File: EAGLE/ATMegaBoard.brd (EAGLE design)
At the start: 71.1 x 54.3 mm, 31 parts, among them IC1 L298, IC2 ATMEGA168-20P, IC3 REG1117, X1 49S/18PF

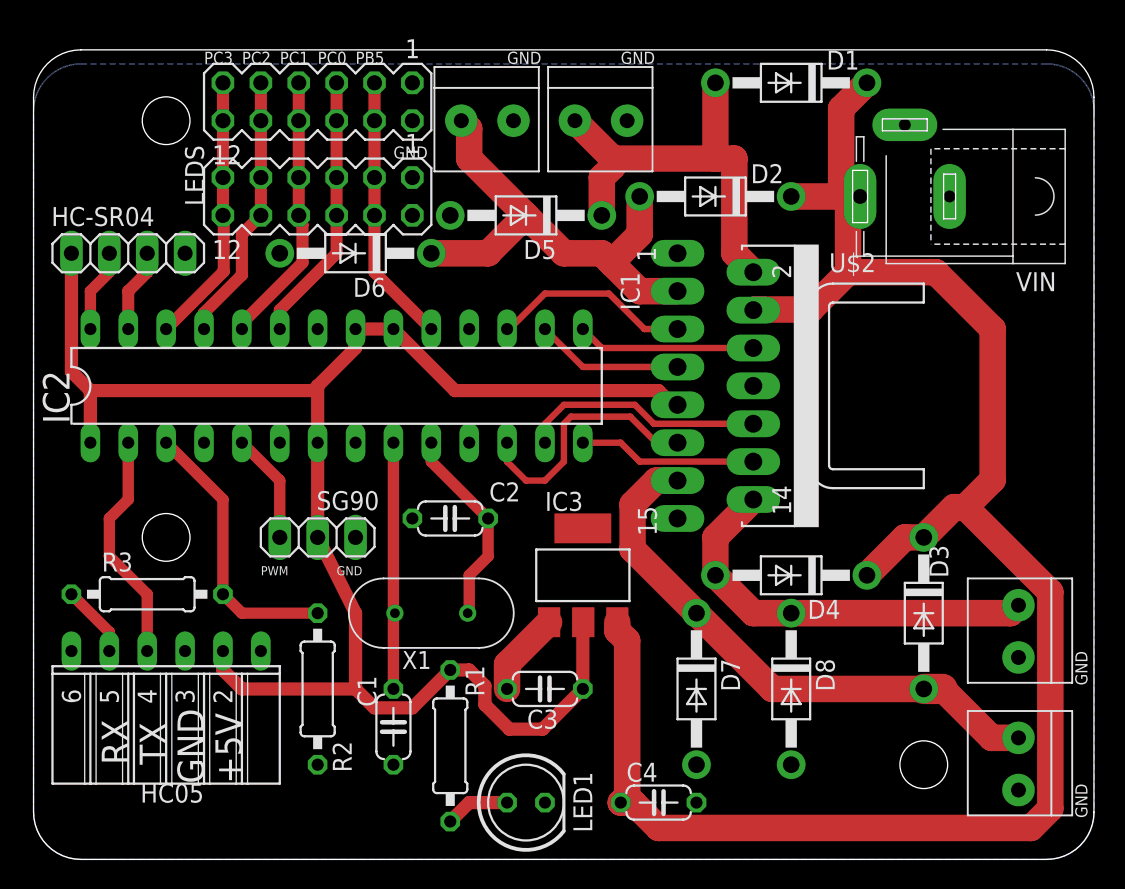
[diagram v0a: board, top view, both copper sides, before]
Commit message: increased clearance between LEDs and D6
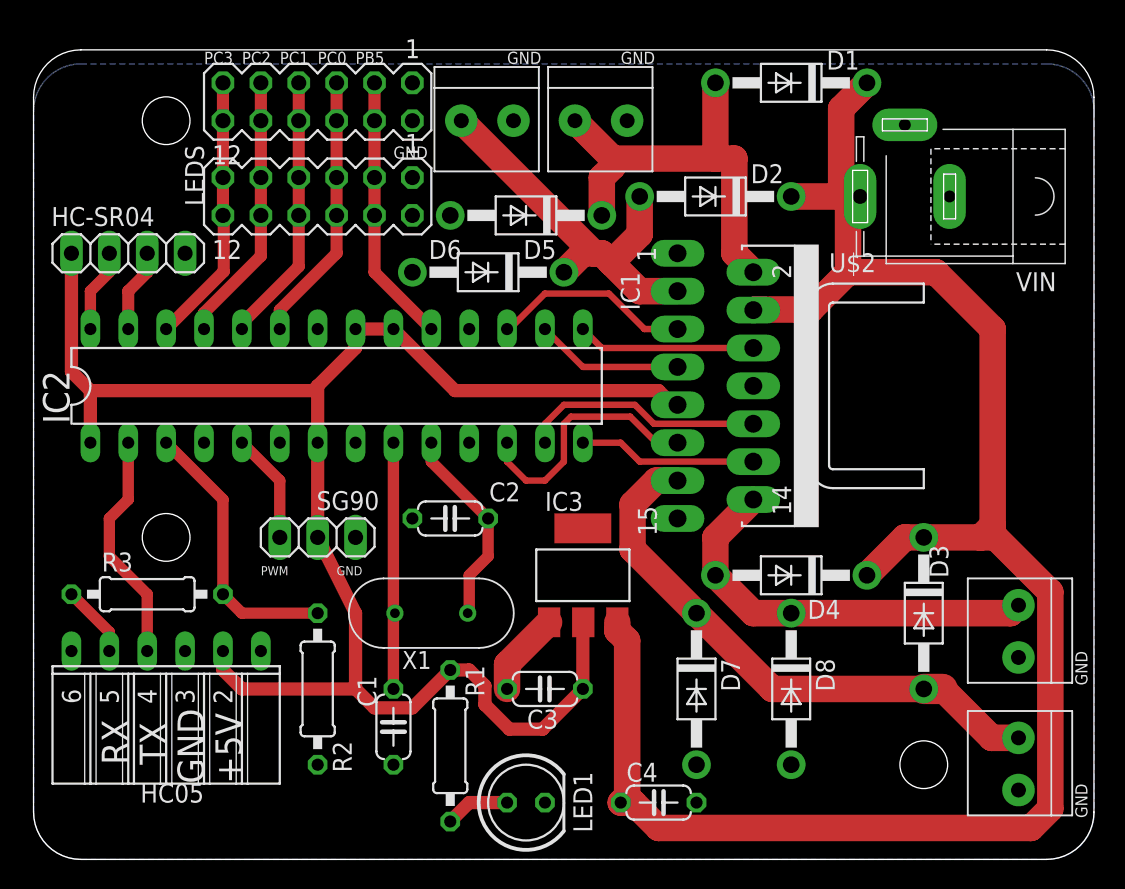
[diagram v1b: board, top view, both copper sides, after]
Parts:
- moved D6 8.98 mm to (30.5, 39.4)
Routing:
- net OUT2: track 33.0 -> 27.0 mm
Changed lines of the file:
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@@
 <drawing>
 <settings>
-<setting alwaysvectorfont="yes"/>
+<setting alwaysvectorfont="no"/>
 <setting verticaltext="up"/>
 </settings>
@@
 <attribute name="VALUE" x="35.052" y="45.974" size="1.27" layer="27" ratio="10" rot="R180"/>
 </element>
-<element name="D6" library="adafruit" package="DO41-10" value="1N4004" x="21.59" y="40.64" smashed="yes" rot="R180">
-<attribute name="NAME" x="23.622" y="38.989" size="1.27" layer="25" ratio="10" rot="R180"/>
-<attribute name="VALUE" x="23.622" y="43.434" size="1.27" layer="27" ratio="10" rot="R180"/>
+<element name="D6" library="adafruit" package="DO41-10" value="1N4004" x="30.48" y="39.37" smashed="yes" rot="R180">
+<attribute name="NAME" x="28.702" y="41.529" size="1.27" layer="25" ratio="10" rot="R180"/>
+<attribute name="VALUE" x="32.512" y="42.164" size="1.27" layer="27" ratio="10" rot="R180"/>
 </element>
 <element name="D7" library="adafruit" package="DO41-10" value="1N4004" x="44.45" y="11.43" smashed="yes" rot="R270">
@@
 <contactref element="C4" pad="1"/>
 <wire x1="48.26" y1="36.83" x2="48.3616" y2="36.8681" width="1.778" layer="1"/>
-<wire x1="64.31" y1="25.4508" x2="64.31" y2="35.56" width="1.778" layer="1"/>
 <wire x1="39.1414" y1="15.3353125" x2="39.8018" y2="14.6749125" width="1.778" layer="1"/>
 <wire x1="39.1414" y1="15.3353125" x2="39.1414" y2="15.9004" width="1.778" layer="1"/>
-<wire x1="62.478284375" y1="23.619084375" x2="64.31" y2="25.4508" width="1.778" layer="1"/>
 <wire x1="54.61" y1="39.37" x2="54.61" y2="44.45" width="1.778" layer="1"/>
 <wire x1="50.8" y1="44.45" x2="54.61" y2="44.45" width="1.778" layer="1"/>
 <wire x1="39.8018" y1="14.6749125" x2="39.8018" y2="4.2418" width="1.778" layer="1"/>
-<wire x1="62.478284375" y1="23.619084375" x2="68.1736" y2="17.92376875" width="1.778" layer="1"/>
-<wire x1="68.1736" y1="3.4036" x2="68.1736" y2="17.92376875" width="1.778" layer="1"/>
+<wire x1="68.1736" y1="17.92376875" x2="68.1736" y2="3.4036" width="1.778" layer="1"/>
 <wire x1="41.91" y1="2.1082" x2="66.8782" y2="2.1082" width="1.778" layer="1"/>
 <wire x1="66.8782" y1="2.1082" x2="68.1736" y2="3.4036" width="1.778" layer="1"/>
-<wire x1="64.31" y1="35.56" x2="60.5" y2="39.37" width="1.778" layer="1"/>
+<wire x1="60.5" y1="39.37" x2="64.31" y2="35.56" width="1.778" layer="1"/>
 <wire x1="60.5" y1="39.37" x2="54.61" y2="39.37" width="1.778" layer="1"/>
 <wire x1="55.42" y1="44.45" x2="54.61" y2="44.45" width="1.778" layer="1"/>
@@
 <wire x1="55.88" y1="19.05" x2="58.42" y2="21.59" width="1.778" layer="1"/>
 <wire x1="58.42" y1="21.59" x2="59.69" y2="21.59" width="1.778" layer="1"/>
-<wire x1="59.69" y1="21.59" x2="61.719084375" y2="23.619084375" width="1.778" layer="1"/>
-<wire x1="61.719084375" y1="23.619084375" x2="62.478284375" y2="23.619084375" width="1.778" layer="1"/>
 <wire x1="52.1081" y1="36.8681" x2="54.61" y2="39.37" width="1.778" layer="1"/>
 <wire x1="48.3616" y1="36.8681" x2="52.1081" y2="36.8681" width="1.778" layer="1"/>
@@
 <wire x1="55.42" y1="44.45" x2="54.15" y2="44.45" width="1.778" layer="1"/>
 <wire x1="55.88" y1="52.07" x2="54.15" y2="50.34" width="1.778" layer="1"/>
+<wire x1="59.69" y1="21.59" x2="63.5" y2="21.59" width="1.778" layer="1"/>
+<wire x1="63.5" y1="21.59" x2="64.50736875" y2="21.59" width="1.778" layer="1"/>
+<wire x1="64.50736875" y1="21.59" x2="68.1736" y2="17.92376875" width="1.778" layer="1"/>
+<wire x1="64.31" y1="22.4" x2="63.5" y2="21.59" width="1.778" layer="1"/>
+<wire x1="64.31" y1="35.56" x2="64.31" y2="22.4" width="1.778" layer="1"/>
 </signal>
 <signal name="IN4">
@@
 <contactref element="D2" pad="A"/>
 <contactref element="D6" pad="C"/>
-<wire x1="35.56" y1="40.64" x2="38.1" y2="40.64" width="1.778" layer="1"/>
+<wire x1="36.83" y1="40.64" x2="37.57" y2="40.64" width="1.778" layer="1"/>
+<wire x1="37.57" y1="40.64" x2="38.1" y2="40.64" width="1.778" layer="1"/>
 <wire x1="40.64" y1="38.1" x2="38.735" y2="40.005" width="1.778" layer="1"/>
 <wire x1="38.735" y1="40.005" x2="38.1" y2="40.64" width="1.778" layer="1"/>
 <wire x1="40.64" y1="38.1" x2="43.18" y2="38.1" width="1.778" layer="1"/>
-<wire x1="29.21" y1="49" x2="28.68" y2="49.53" width="1.778" layer="1"/>
-<wire x1="29.21" y1="46.99" x2="29.21" y2="49" width="1.778" layer="1"/>
 <wire x1="40.64" y1="44.45" x2="40.64" y2="41.91" width="1.778" layer="1"/>
 <wire x1="40.64" y1="41.91" x2="38.735" y2="40.005" width="1.778" layer="1"/>
-<wire x1="35.56" y1="40.64" x2="33.02" y2="43.18" width="1.778" layer="1"/>
-<wire x1="33.02" y1="43.18" x2="29.21" y2="46.99" width="1.778" layer="1"/>
-<wire x1="26.67" y1="40.64" x2="30.48" y2="40.64" width="1.778" layer="1"/>
-<wire x1="30.48" y1="40.64" x2="33.02" y2="43.18" width="1.778" layer="1"/>
+<wire x1="37.57" y1="40.64" x2="28.68" y2="49.53" width="1.778" layer="1"/>
+<wire x1="35.56" y1="39.37" x2="36.83" y2="40.64" width="1.778" layer="1"/>
 </signal>
 <signal name="OUT3" class="1">
@@
 <contactref element="LIGHTS1" pad="7"/>
 <contactref element="LIGHTS1" pad="8"/>
-<wire x1="18.034" y1="40.0087375" x2="18.034" y2="42.5412625" width="0.8128" layer="1"/>
-<wire x1="18.034" y1="42.5412625" x2="17.78" y2="42.7952625" width="0.8128" layer="1"/>
-<wire x1="17.78" y1="42.7952625" x2="17.78" y2="43.18" width="0.8128" layer="1"/>
+<wire x1="17.78" y1="39.7547375" x2="17.78" y2="43.18" width="0.8128" layer="1"/>
 <wire x1="13.97" y1="35.56" x2="13.97" y2="35.9447375" width="0.8128" layer="1"/>
-<wire x1="13.97" y1="35.9447375" x2="18.034" y2="40.0087375" width="0.8128" layer="1"/>
+<wire x1="13.97" y1="35.9447375" x2="17.78" y2="39.7547375" width="0.8128" layer="1"/>
 <wire x1="17.78" y1="43.18" x2="17.78" y2="45.72" width="0.8128" layer="1"/>
 <wire x1="17.78" y1="45.72" x2="17.78" y2="49.53" width="0.8128" layer="1"/>
@@
 <contactref element="LEDS" pad="10"/>
 <contactref element="IC2" pad="25"/>
+<wire x1="15.24" y1="40.45510625" x2="11.43" y2="36.64510625" width="0.8128" layer="1"/>
 <wire x1="11.43" y1="35.56" x2="11.43" y2="36.64510625" width="0.8128" layer="1"/>
-<wire x1="13.97" y1="39.18510625" x2="11.43" y2="36.64510625" width="0.8128" layer="1"/>
-<wire x1="13.97" y1="41.91" x2="13.97" y2="39.18510625" width="0.8128" layer="1"/>
-<wire x1="13.97" y1="41.91" x2="15.24" y2="43.18" width="0.8128" layer="1"/>
+<wire x1="15.24" y1="43.18" x2="15.24" y2="40.45510625" width="0.8128" layer="1"/>
 <wire x1="15.24" y1="43.18" x2="15.24" y2="45.72" width="0.8128" layer="1"/>
 <wire x1="15.24" y1="45.72" x2="15.24" y2="49.53" width="0.8128" layer="1"/>

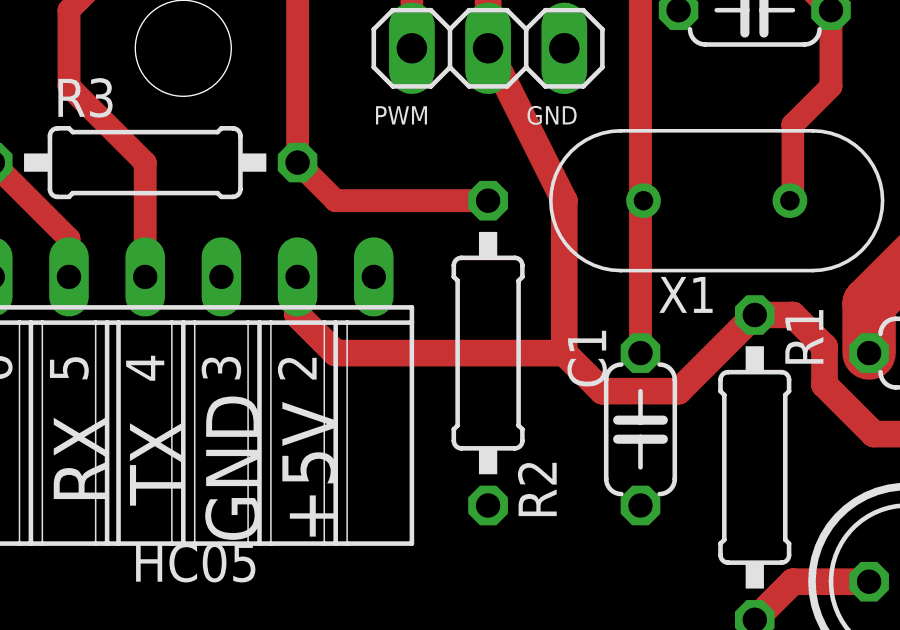
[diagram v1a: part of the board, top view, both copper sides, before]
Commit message: set EN on HC-05 to +5v
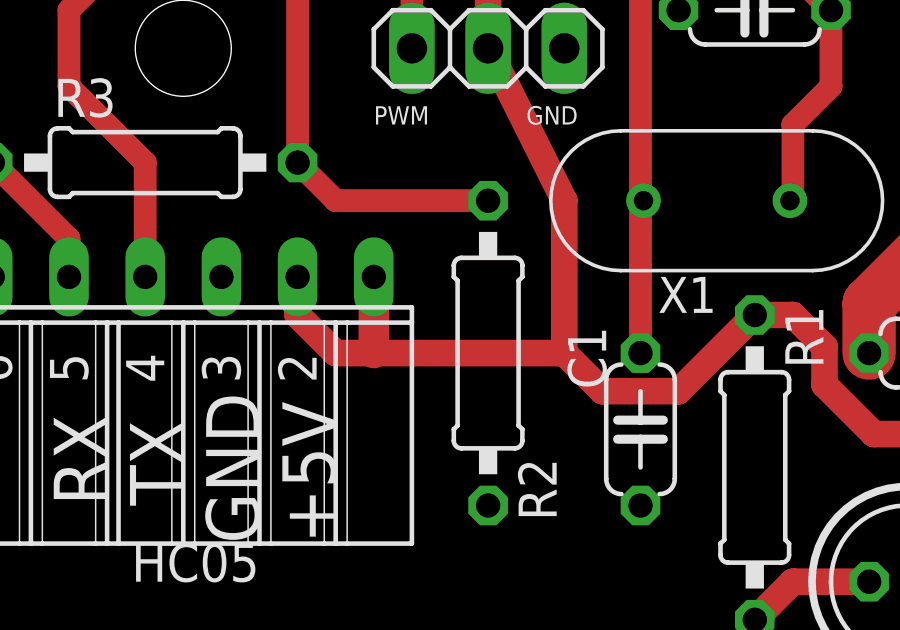
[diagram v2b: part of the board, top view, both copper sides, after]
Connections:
- net +5V: now also HC05.1
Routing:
- net +5V: track 113.6 -> 116.1 mm
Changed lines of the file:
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@@
 <wire x1="36.83" y1="15.875" x2="36.8554" y2="15.9004" width="0.889" layer="1"/>
 <wire x1="3.81" y1="27.94" x2="3.81" y2="31.4325" width="0.889" layer="1"/>
-<wire x1="21.59" y1="11.43" x2="13.97" y2="11.43" width="0.889" layer="1"/>
+<wire x1="21.59" y1="11.43" x2="15.24" y2="11.43" width="0.889" layer="1"/>
+<wire x1="15.24" y1="11.43" x2="13.97" y2="11.43" width="0.889" layer="1"/>
 <wire x1="13.97" y1="11.43" x2="12.7" y2="12.7" width="0.889" layer="1"/>
 <wire x1="21.59" y1="11.43" x2="22.86" y2="10.16" width="0.889" layer="1"/>
+<contactref element="HC05" pad="1"/>
+<wire x1="15.24" y1="13.97" x2="15.24" y2="11.43" width="1.016" layer="1"/>
 </signal>
 <signal name="GND" class="1">
